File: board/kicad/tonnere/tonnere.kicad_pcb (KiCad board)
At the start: 6 copper layers, 256.2 x 141.3 mm, 404 parts, among them J10 STM SWD, J12 Conn_01x05, J14 STM USART TTL, J15 SPI CFG, J17 SPI SEL, J18 FPGA GPIO, J19 ESP PGM, J20 USB_A, J21 73725-1180RLF, J22 FPGA JTAG, J23 ESP JTAG, J24 CONSOL, J25 73725-1180RLF, J26 73725-1180RLF, J27 I2C, J28 JA23331-HA6Q-4F, J4 DE15_Pins_HighDensity_Mountin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, J5 HDMI_A, J6 PBI, J7 Conn_01x01, J8 PBI Option, J9 STM GPIO, Q1 BCX51, Q2 DMN2058U, Q3 2N7002, SW1 SA-0-102-C04-0004-WP, SW2 USB HS/FS, U1 TPD4E02B04DQA, U10 TPD8E003DQDR, U11 74LVC1G17, U12 TPD4E02B04DQA, U13 TPD8E003DQDR, U14 TPD8E003DQDR, U15 TPS62903RPJR, U16 TPS62903RPJR, U17 FSUSB42UMX-TP, U18 TPD8E003DQDR, U19 PCM5102A, U2 TPD4E02B04DQA, U20 USB3300-EZK, U21 FSUSB42UMX-TP, U22 TPS62903RPJR, U23 STM32F407ZGTx, U24 TPD8E003DQDR, U25 THS7316DR, U26 PCA9546APWR, U27 M25PX32-VMW, U28 TPD8E003DQDR, U29 M25PX32-VMW, U3 TPD4E02B04DQA, U30 SN74CB3T16211DGVR, U31 IS61WV204816BLL-10BLI, U32 SN74CB3T16211DGVR, U33 10CL040f484, U34 AP2553AW6-7, U35 SN74CB3T16211DGVR, U36 IS61WV204816BLL-10BLI, U37 SN74CB3T16211DGVR, U38 AP2553AW6-7, U39 AP2553AW6-7, U4 TPD4E02B04DQA, U40 ESP32-WROVER-E-N8R8, U41 AP2553AW6-7, U42 AS4C16M16SA, U43 TPD4E02B04DQA, U44 USB2514B_Bi, U45 TPD4E02B04DQA, U46 TPD4E02B04DQA, U47 TPD4E02B04DQA, U48 PLT237/T10WH, U5 TPD8E003DQDR, U6 TPD8E003DQDR, U7 TPD8E003DQDR, U8 TPD8E003DQDR, U9 TPD8E003DQDR, Y1 24MHz, Y2 8MHz, Y3 32.768KHz, Y4 25MHz, Y5 Si5351A-B-GT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

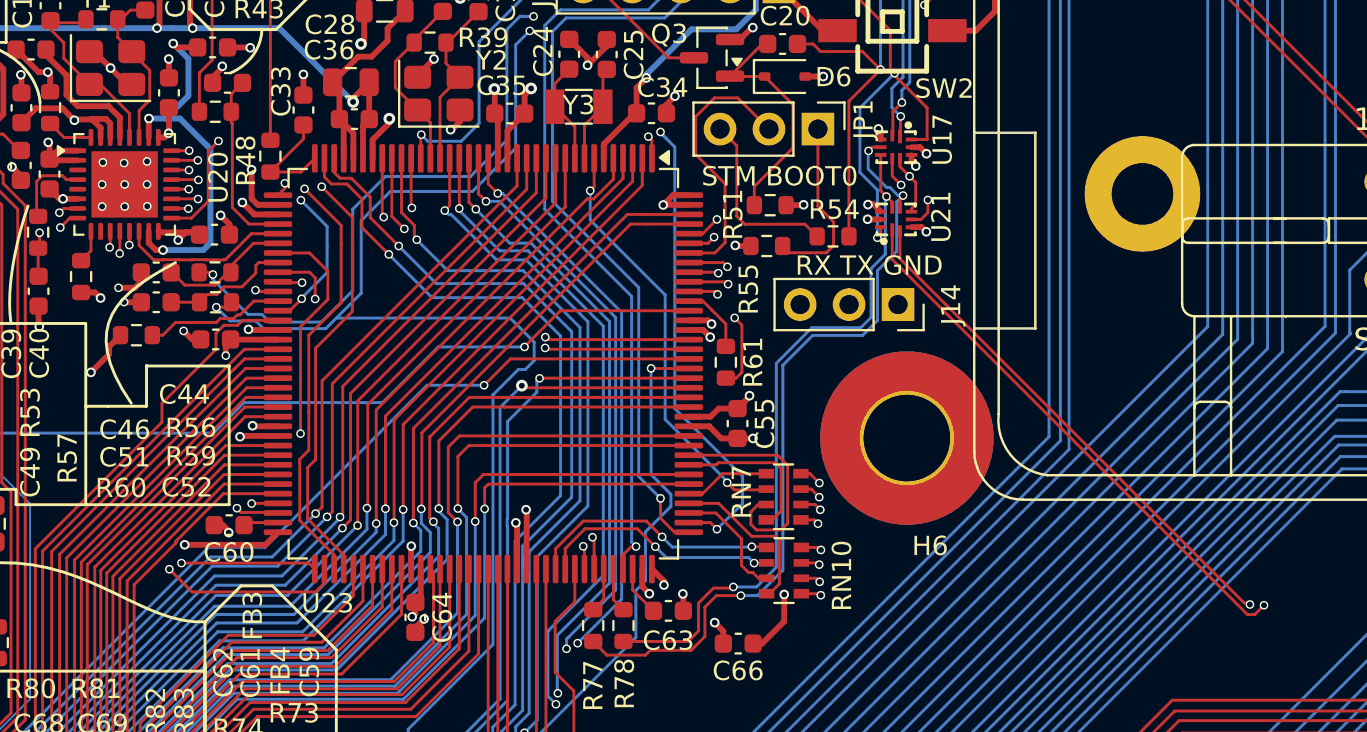
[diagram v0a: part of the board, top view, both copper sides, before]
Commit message: Moved ADC pins around in order to have a dummy rank to stop bleed at high frequency sampling
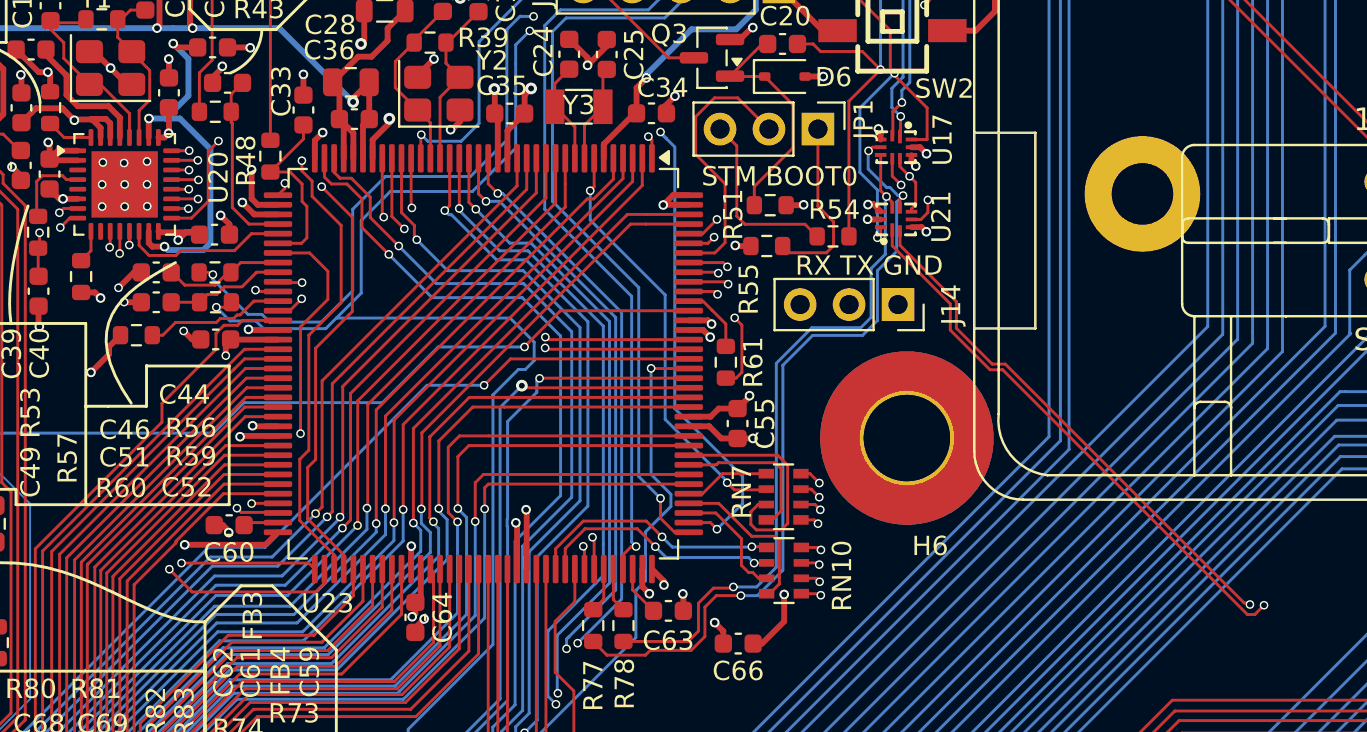
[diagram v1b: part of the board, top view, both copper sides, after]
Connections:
- J9 pad 3: Net-(J9-Pin_3) -> unconnected-(J9-Pin_3-Pad3)
- U23 pad 36: /Audio/STMAUD.ADC.L -> GND
- U23 pad 42: /Audio/STMAUD.ADC.PBI -> /Audio/STMAUD.ADC.L
- U23 pad 44: /Audio/STMAUD.ADC.SIO -> /Audio/STMAUD.ADC.PBI
- U23 pad 45: /Microcontroller/STM.I2CRESET -> /Audio/STMAUD.ADC.SIO
- U23 pad 49: Net-(J9-Pin_3) -> /Microcontroller/STM.I2CRESET
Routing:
- net Net-(J9-Pin_3): track 34.2 -> 0.00 mm, vias 2 -> 0
- net /Audio/STMAUD.ADC.L: track 5.76 -> 9.63 mm
- net /Microcontroller/STM.I2CRESET: track 61.3 -> 59.5 mm
- net GND: track 542.9 -> 544.1 mm, vias 343 -> 344
- net /Audio/STMAUD.ADC.PBI: track 6.97 -> 6.30 mm
